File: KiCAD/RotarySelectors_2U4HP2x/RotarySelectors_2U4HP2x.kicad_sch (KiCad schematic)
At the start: 8 parts, among them J1 Conn_01x08_Socket, J2 Conn_01x01_Socket, J3 Conn_01x08_Socket, J4 Conn_01x01_Socket

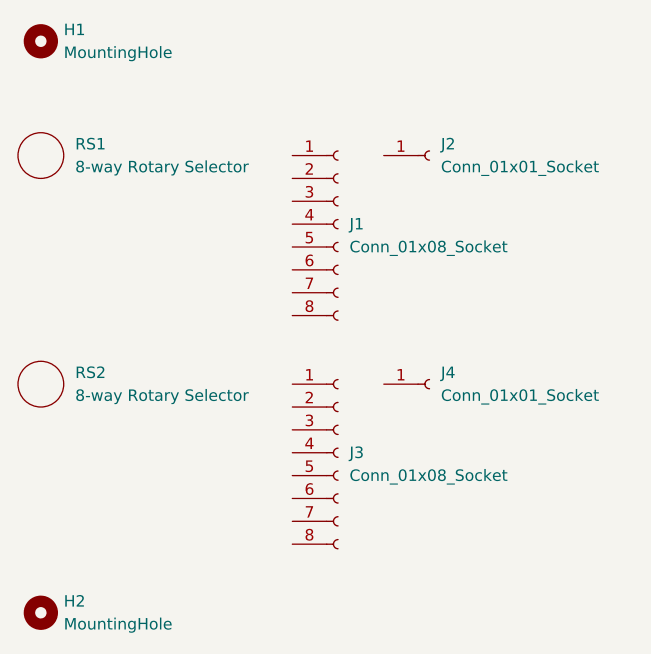
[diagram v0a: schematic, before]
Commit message: updated PCB widths to better conform to Eurorack standards
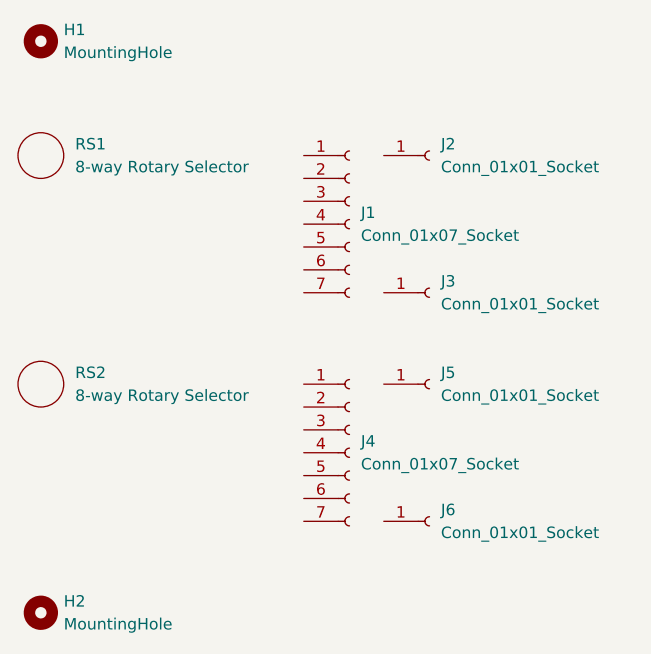
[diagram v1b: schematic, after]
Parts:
- removed J1, J3: Conn_01x08_Socket, Connector_PinSocket_2.54mm:PinSocket_1x08_P2.54mm_Vertical, symbol Connector:Conn_01x08_Socket
- added J1, J4: Conn_01x07_Socket, Connector_PinSocket_2.54mm:PinSocket_1x07_P2.54mm_Vertical, symbol Connector:Conn_01x07_Socket
- added J3, J6: Conn_01x01_Socket, Connector_PinSocket_2.54mm:PinSocket_1x01_P2.54mm_Vertical, symbol Connector:Conn_01x01_Socket
- renumbered J4 to J5
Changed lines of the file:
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@@
 		(dnp no)
 		(fields_autoplaced yes)
-		(property "Reference" "J4"
+		(property "Reference" "J5"
 			(at 69.85 62.2299 0)
 			(effects
@@
 			(project "RotarySelectors_2U4HP2x"
 				(path "/0e198784-194e-44f0-aeec-16cede6cf8f3"
-					(reference "J4")
+					(reference "J5")
 					(unit 1)
 				)
@@
 	)
 	(symbol
+		(lib_id "Connector:Conn_01x07_Socket")
+		(at 59.69 45.72 0)
+		(unit 1)
+		(exclude_from_sim no)
+		(in_bom yes)
+		(on_board yes)
+		(dnp no)
+		(fields_autoplaced yes)
+		(property "Reference" "J1"
+			(at 60.96 44.4499 0)
+			(effects
+				(font
+					(size 1.27 1.27)
+				)
+				(justify left)
+			)
+		)
+		(property "Value" "Conn_01x07_Socket"
+			(at 60.96 46.9899 0)
+			(effects
+				(font
+					(size 1.27 1.27)
+				)
+				(justify left)
+			)
+		)
+		(property "Footprint" "Connector_PinSocket_2.54mm:PinSocket_1x07_P2.54mm_Vertical"
+			(at 59.69 45.72 0)
+			(effects
+				(font
+					(size 1.27 1.27)
+				)
+				(hide yes)
+			)
+		)
+		(property "Datasheet" "~"
+			(at 59.69 45.72 0)
+			(effects
+				(font
+					(size 1.27 1.27)
+				)
+				(hide yes)
+			)
+		)
+		(property "Description" "Generic connector, single row, 01x07, script generated"
+			(at 59.69 45.72 0)
+			(effects
+				(font
+					(size 1.27 1.27)
+				)
+				(hide yes)
+			)
+		)
+		(pin "5"
+		)
+		(pin "6"
+		)
+		(pin "1"
+		)
+		(pin "3"
+		)
+		(pin "2"
+		)
+		(pin "4"
+		)
+		(pin "7"
+		)
+		(instances
+			(project ""
+				(path "/0e198784-194e-44f0-aeec-16cede6cf8f3"
+					(reference "J1")
+					(unit 1)
+				)
+			)
+		)
+	)
+	(symbol
+		(lib_id "Connector:Conn_01x01_Socket")
+		(at 68.58 78.74 0)
+		(unit 1)
+		(exclude_from_sim no)
+		(in_bom yes)
+		(on_board yes)
+		(dnp no)
+		(fields_autoplaced yes)
+		(property "Reference" "J6"
+			(at 69.85 77.4699 0)
+			(effects
+				(font
+					(size 1.27 1.27)
+				)
+				(justify left)
+			)
+		)
+		(property "Value" "Conn_01x01_Socket"
+			(at 69.85 80.0099 0)
+			(effects
+				(font
+					(size 1.27 1.27)
+				)
+				(justify left)
+			)
+		)
+		(property "Footprint" "Connector_PinSocket_2.54mm:PinSocket_1x01_P2.54mm_Vertical"
+			(at 68.58 78.74 0)
+			(effects
+				(font
+					(size 1.27 1.27)
+				)
+				(hide yes)
+			)
+		)
+		(property "Datasheet" "~"
+			(at 68.58 78.74 0)
+			(effects
+				(font
+					(size 1.27 1.27)
+				)
+				(hide yes)
+			)
+		)
+		(property "Description" "Generic connector, single row, 01x01, script generated"
+			(at 68.58 78.74 0)
+			(effects
+				(font
+					(size 1.27 1.27)
+				)
+				(hide yes)
+			)
+		)
+		(pin "1"
+		)
+		(instances
+			(project "RotarySelectors_2U4HP2x"
+				(path "/0e198784-194e-44f0-aeec-16cede6cf8f3"
+					(reference "J6")
+					(unit 1)
+				)
+			)
+		)
+	)
+	(symbol
 		(lib_id "Connector:Conn_01x01_Socket")
 		(at 68.58 38.1 0)
@@
 	)
 	(symbol
-		(lib_id "Connector:Conn_01x08_Socket")
-		(at 58.42 45.72 0)
+		(lib_id "Connector:Conn_01x07_Socket")
+		(at 59.69 71.12 0)
 		(unit 1)
 		(exclude_from_sim no)
@@
 		(dnp no)
 		(fields_autoplaced yes)
-		(property "Reference" "J1"
-			(at 59.69 45.7199 0)
-			(effects
-				(font
-					(size 1.27 1.27)
-				)
-				(justify left)
-			)
-		)
-		(property "Value" "Conn_01x08_Socket"
-			(at 59.69 48.2599 0)
-			(effects
-				(font
-					(size 1.27 1.27)
-				)
-				(justify left)
-			)
-		)
-		(property "Footprint" "Connector_PinSocket_2.54mm:PinSocket_1x08_P2.54mm_Vertical"
-			(at 58.42 45.72 0)
-			(effects
-				(font
-					(size 1.27 1.27)
-				)
-				(hide yes)
-			)
-		)
-		(property "Datasheet" "~"
-			(at 58.42 45.72 0)
-			(effects
-				(font
-					(size 1.27 1.27)
-				)
-				(hide yes)
-			)
-		)
-		(property "Description" "Generic connector, single row, 01x08, script generated"
-			(at 58.42 45.72 0)
-			(effects
-				(font
-					(size 1.27 1.27)
-				)
-				(hide yes)
-			)
+		(property "Reference" "J4"
+			(at 60.96 69.8499 0)
+			(effects
+				(font
+					(size 1.27 1.27)
+				)
+				(justify left)
+			)
+		)
+		(property "Value" "Conn_01x07_Socket"
+			(at 60.96 72.3899 0)
+			(effects
+				(font
+					(size 1.27 1.27)
+				)
+				(justify left)
+			)
+		)
+		(property "Footprint" "Connector_PinSocket_2.54mm:PinSocket_1x07_P2.54mm_Vertical"
+			(at 59.69 71.12 0)
+			(effects
+				(font
+					(size 1.27 1.27)
+				)
+				(hide yes)
+			)
+		)
+		(property "Datasheet" "~"
+			(at 59.69 71.12 0)
+			(effects
+				(font
+					(size 1.27 1.27)
+				)
+				(hide yes)
+			)
+		)
+		(property "Description" "Generic connector, single row, 01x07, script generated"
+			(at 59.69 71.12 0)
+			(effects
+				(font
+					(size 1.27 1.27)
+				)
+				(hide yes)
+			)
+		)
+		(pin "5"
 		)
 		(pin "6"
 		)
+		(pin "1"
+		)
 		(pin "3"
 		)
 		(pin "2"
 		)
-		(pin "8"
-		)
-		(pin "1"
-		)
-		(pin "5"
-		)
 		(pin "4"
 		)
@@
 		)
 		(instances
-			(project ""
-				(path "/0e198784-194e-44f0-aeec-16cede6cf8f3"
-					(reference "J1")
-					(unit 1)
-				)
-			)
-		)
-	)
-	(symbol
-		(lib_id "Connector:Conn_01x08_Socket")
-		(at 58.42 71.12 0)
+			(project "RotarySelectors_2U4HP2x"
+				(path "/0e198784-194e-44f0-aeec-16cede6cf8f3"
+					(reference "J4")
+					(unit 1)
+				)
+			)
+		)
+	)
+	(symbol
+		(lib_id "Connector:Conn_01x01_Socket")
+		(at 68.58 53.34 0)
 		(unit 1)
 		(exclude_from_sim no)
@@
 		(fields_autoplaced yes)
 		(property "Reference" "J3"
-			(at 59.69 71.1199 0)
-			(effects
-				(font
-					(size 1.27 1.27)
-				)
-				(justify left)
-			)
-		)
-		(property "Value" "Conn_01x08_Socket"
-			(at 59.69 73.6599 0)
-			(effects
-				(font
-					(size 1.27 1.27)
-				)
-				(justify left)
-			)
-		)
-		(property "Footprint" "Connector_PinSocket_2.54mm:PinSocket_1x08_P2.54mm_Vertical"
-			(at 58.42 71.12 0)
-			(effects
-				(font
-					(size 1.27 1.27)
-				)
-				(hide yes)
-			)
-		)
-		(property "Datasheet" "~"
-			(at 58.42 71.12 0)
-			(effects
-				(font
-					(size 1.27 1.27)
-				)
-				(hide yes)
-			)
-		)
-		(property "Description" "Generic connector, single row, 01x08, script generated"
-			(at 58.42 71.12 0)
-			(effects
-				(font
-					(size 1.27 1.27)
-				)
-				(hide yes)
-			)
-		)
-		(pin "6"
-		)
-		(pin "3"
-		)
-		(pin "2"
-		)
-		(pin "8"
+			(at 69.85 52.0699 0)
+			(effects
+				(font
+					(size 1.27 1.27)
+				)
+				(justify left)
+			)
+		)
+		(property "Value" "Conn_01x01_Socket"
+			(at 69.85 54.6099 0)
+			(effects
+				(font
+					(size 1.27 1.27)
+				)
+				(justify left)
+			)
+		)
+		(property "Footprint" "Connector_PinSocket_2.54mm:PinSocket_1x01_P2.54mm_Vertical"
+			(at 68.58 53.34 0)
+			(effects
+				(font
+					(size 1.27 1.27)
+				)
+				(hide yes)
+			)
+		)
+		(property "Datasheet" "~"
+			(at 68.58 53.34 0)
+			(effects
+				(font
+					(size 1.27 1.27)
+				)
+				(hide yes)
+			)
+		)
+		(property "Description" "Generic connector, single row, 01x01, script generated"
+			(at 68.58 53.34 0)
+			(effects
+				(font
+					(size 1.27 1.27)
+				)
+				(hide yes)
+			)
 		)
 		(pin "1"
 		)
-		(pin "5"
-		)
-		(pin "4"
-		)
-		(pin "7"
-		)
-		(instances
+		(instances
